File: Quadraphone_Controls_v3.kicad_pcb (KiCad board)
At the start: 2 copper layers, 60 x 110 mm, 32 parts, among them J1 Conn_01x10_Female, J10 Pitch_In, J11 Mix_Out, J13 Conn_01x04_Male, J14 Conn_01x01_Male, J2 Conn_01x10_Female, J3 Conn_01x10_Female, J4 Conn_01x10_Female, J5 PWM_CV, J6 LFO_IN, J7 PWM_CV_In, J8 Synch_Signal_In, J9 Freq_Mod_In, SW1 Synch_Type, SW2 Output_Type, SW3 Output_Type

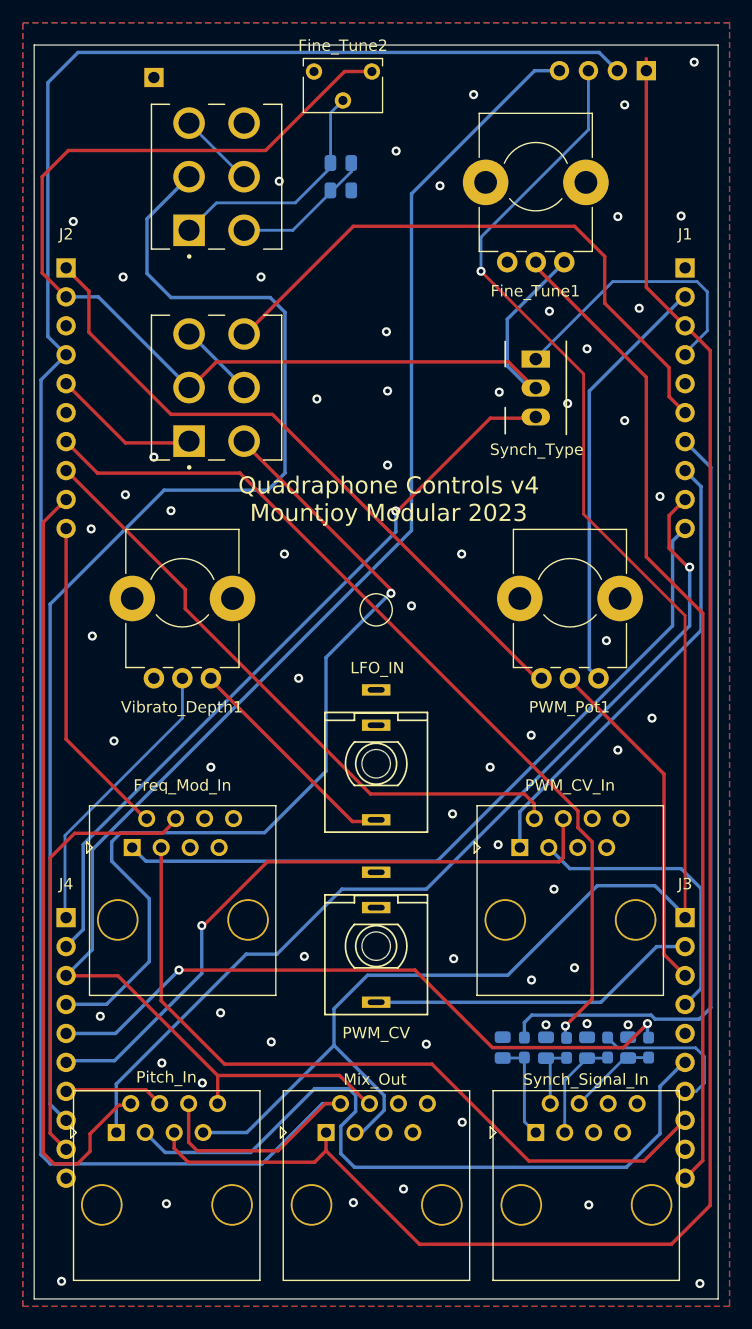
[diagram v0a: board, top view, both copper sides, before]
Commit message: Updates to controls Synch input protection
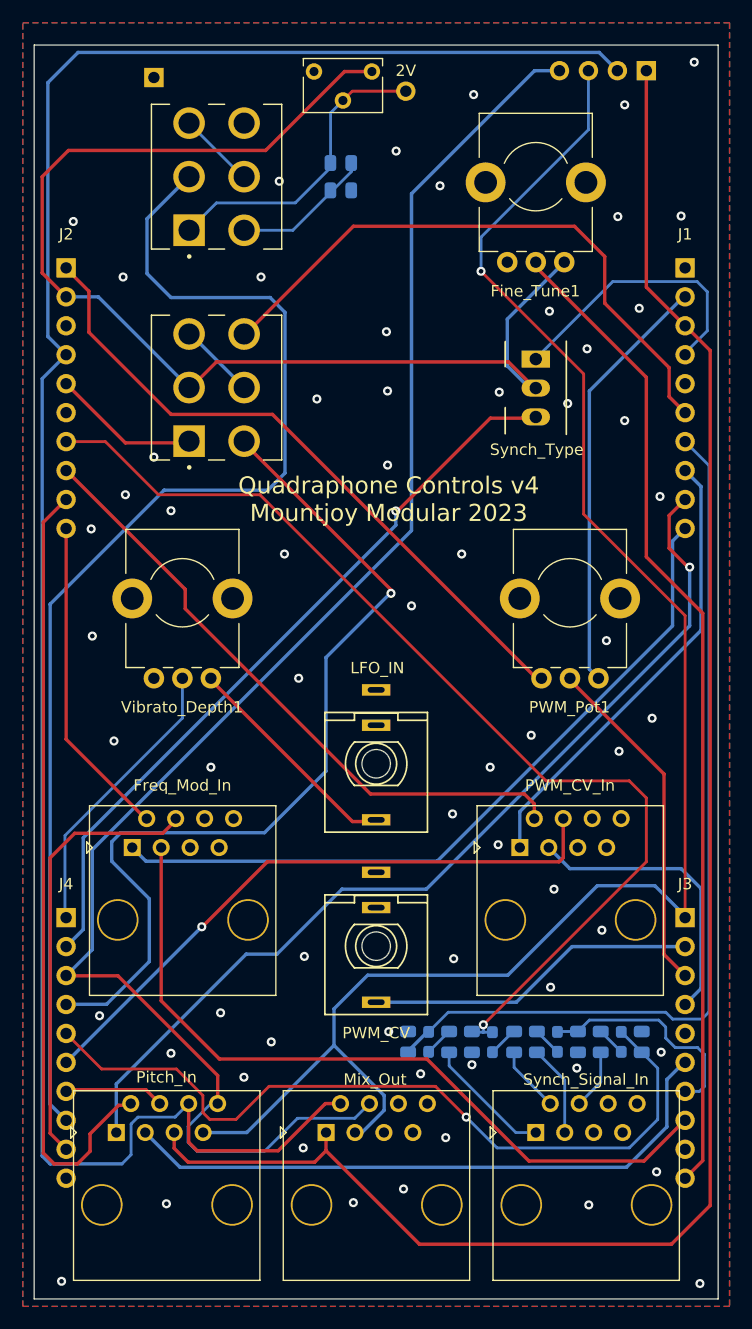
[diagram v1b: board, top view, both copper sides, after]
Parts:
- removed D1: 3d_Model_Components, Custom_Footprints:3D_Dummy
- removed D2: 3d_Model_Panel, Custom_Footprints:3D_Dummy
- removed the R4 at (94.9, 131.4)
- added R10: 12k, Resistor_SMD:R_0805_2012Metric, B.Cu at (103.3, 130.9)
- added R3: 10k, Resistor_SMD:R_0805_2012Metric, B.Cu at (86.4, 130.9)
- added R7: 10k, Resistor_SMD:R_0805_2012Metric, B.Cu at (94.1, 130.9)
- added R8: 12k, Resistor_SMD:R_0805_2012Metric, B.Cu at (97.7, 130.9)
- added R9: 10k, Resistor_SMD:R_0805_2012Metric, B.Cu at (99.7, 130.9)
- added TP1: 2V_Test, Custom_Footprints:1mm_Test_Point, F.Cu at (82.6, 47.5)
- R4: renamed from R3; value 10k -> 12k
- R6: value 10k -> 12k
- moved R6 13.7 mm to (88.4, 130.9), turned to -90 degrees
- moved D3 8.41 mm to (84.6, 130.9)
- moved R4 8.32 mm to (82.8, 130.9)
- moved D4 6.52 mm to (90.2, 130.9)
- moved R5 6.42 mm to (92.1, 130.9)
- moved D5 4.43 mm to (95.9, 130.9)
- moved D6 2.45 mm to (101.5, 130.9)
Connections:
- D3 pad 2: /SYNCH_SIGNAL1 -> Net-(D3-A)
- D4 pad 2: /SYNCH_SIGNAL2 -> Net-(D4-A)
- D5 pad 2: /SYNCH_SIGNAL3 -> Net-(D5-A)
- D6 pad 2: /SYNCH_SIGNAL4 -> Net-(D6-A)
- R4 pad 1: /SYNCH_SIGNAL1 -> /Synch1
- R5 pad 1: /SYNCH_SIGNAL3 -> /SYNCH_SIGNAL2
- R5 pad 2: GND -> Net-(D4-A)
- R6 pad 1: /SYNCH_SIGNAL4 -> /Synch2
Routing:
- net /Synch2: track 79.7 -> 92.1 mm
- net /MIX_OUT2: track 194.7 -> 182.9 mm
- net /Synch4: track 58.3 -> 69.4 mm, vias 2 -> 1
- net /Synch1: track 69.1 -> 79.3 mm
- net /V_PER_OCT3: track 64.3 -> 54.9 mm
- net /MIX_OUT4: track 132.5 -> 140.9 mm
- net /Synch3: track 13.5 -> 19.8 mm
- net /2V: track 21.0 -> 26.9 mm
- net Net-(D4-A): track 0.00 -> 2.65 mm
- net Net-(D5-A): track 0.00 -> 2.54 mm
- net Net-(D6-A): track 0.00 -> 2.54 mm
- net Net-(D3-A): track 0.00 -> 2.53 mm
- net /SYNCH_SIGNAL4: track 7.76 -> 5.28 mm
- net /PWM_CV4: track 56.8 -> 54.3 mm
- net /SYNCH_SIGNAL1: track 8.93 -> 11.2 mm
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
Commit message: Updated resistor values in VCO tuning circuits
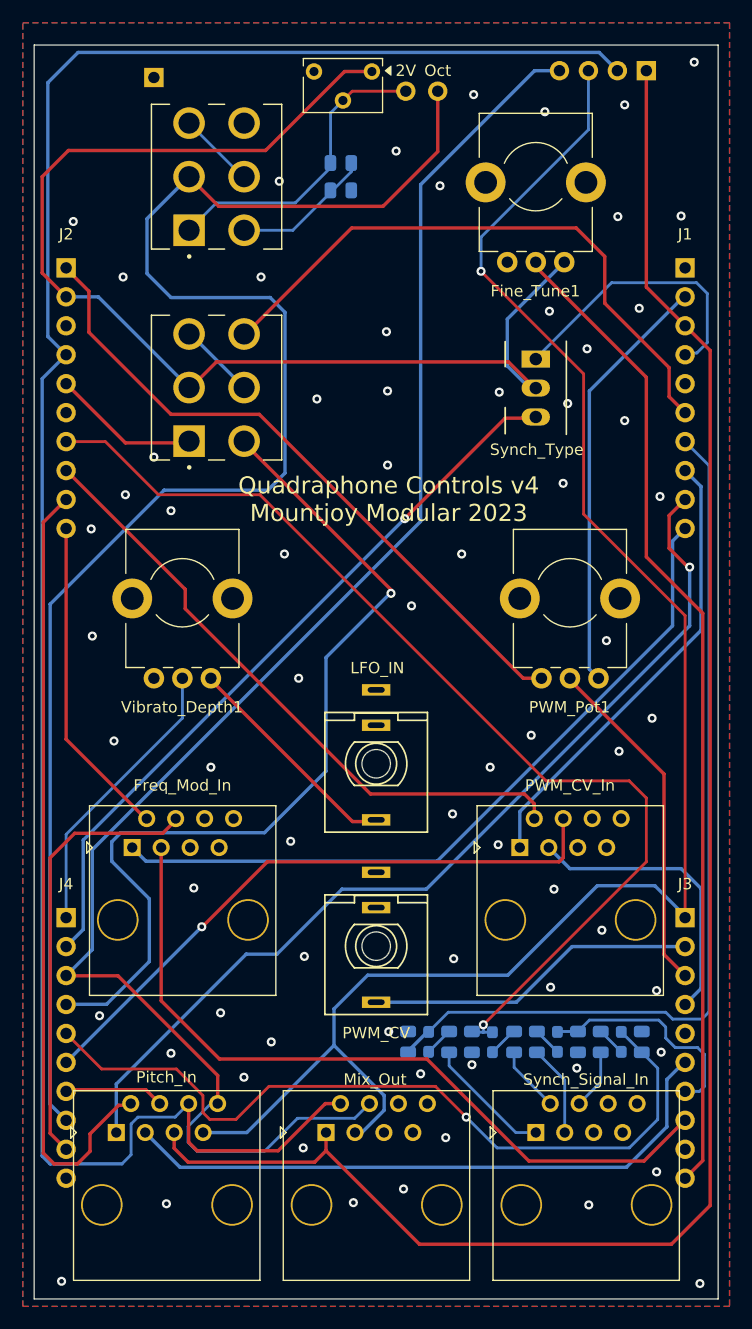
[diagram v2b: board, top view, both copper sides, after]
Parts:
- added TP2: OctTest, Custom_Footprints:1mm_Test_Point, F.Cu at (85.4, 47.5)
- renumbered Fine_Tune2 to OctaveTrim1
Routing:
- net /OCT_TUNE: track 108.9 -> 139.0 mm
- net /SOFT_SYNCH_SW: track 65.9 -> 65.0 mm
- net GND: vias 64 -> 69

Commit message: Gerbers Prepared and Ordered
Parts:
- OctaveTrim1: moved to B.Cu
- moved OctaveTrim1 4.95 mm to (74.7, 45.8), turned to 180 degrees
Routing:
- net GND: track 0.40 -> 3.03 mm
- net +5V: track 105.1 -> 103.0 mm
